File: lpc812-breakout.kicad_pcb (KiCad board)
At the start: 2 copper layers, 24 x 37.5 mm, 28 parts, among them J1 SWD, J2 Left, J3 Right, Q1 BC847BDW1, SW1 Reset, U1 LPC812M101JDH20, Y1 8MHz

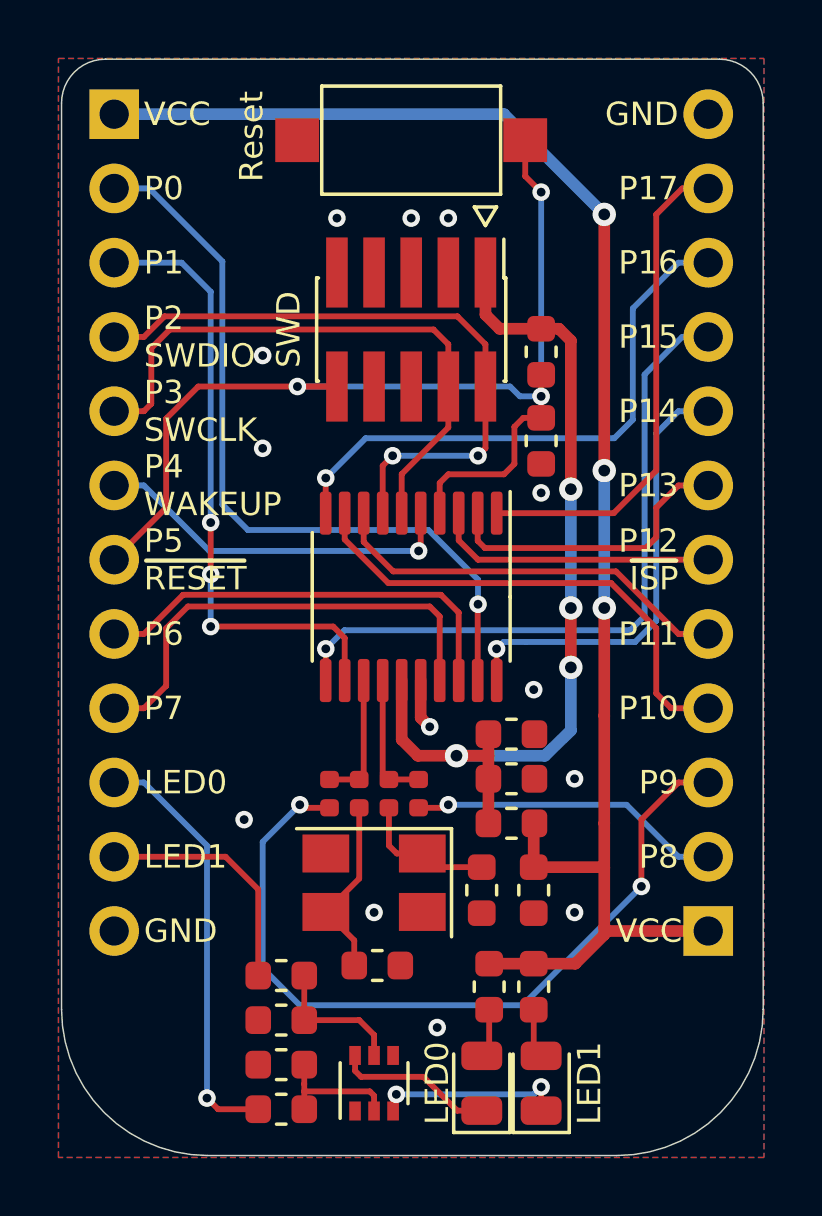
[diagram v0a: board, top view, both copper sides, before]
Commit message: PCB tweaks, updated documentation
- made the PCB a bit narrower: 24 mm -> 23 mm
- added/moved some of the GND vias
- updated docs and the BOM
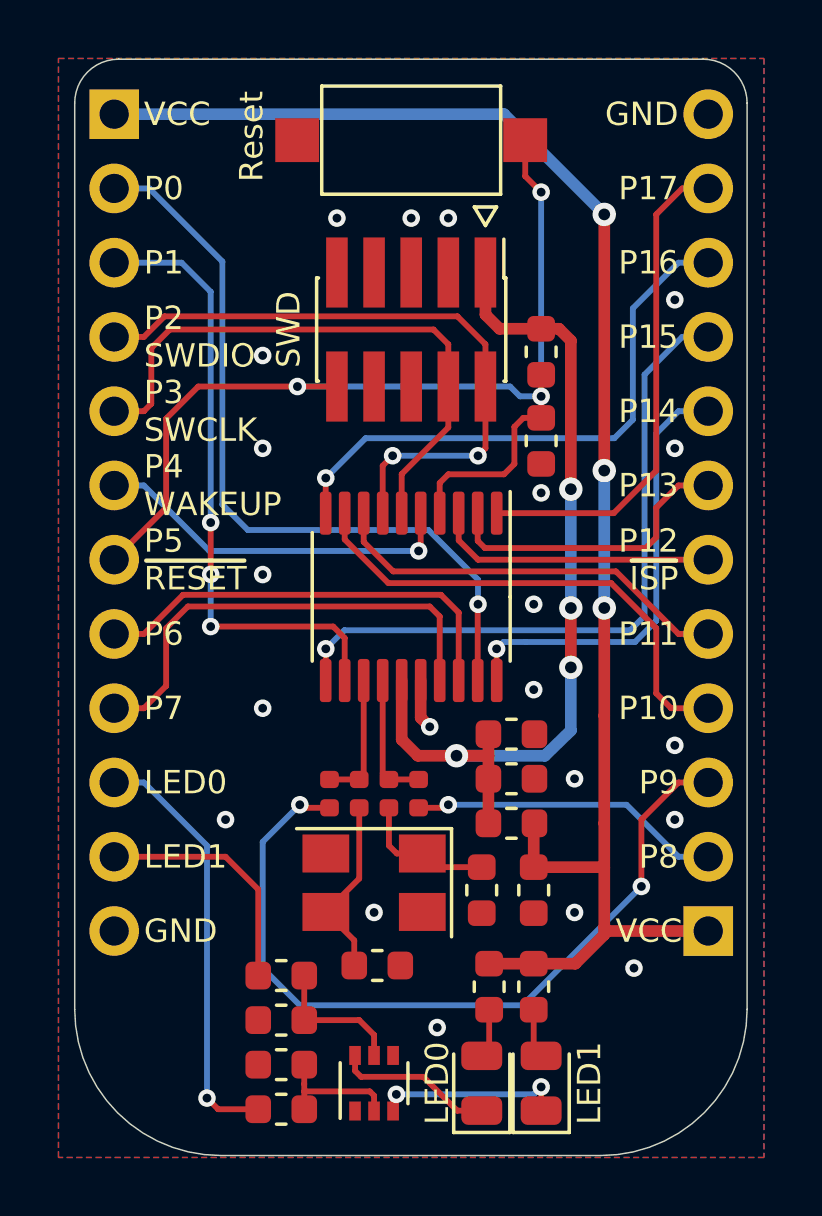
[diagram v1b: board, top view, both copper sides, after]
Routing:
- net GND: vias 13 -> 21
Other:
- board size 24 x 37.5 mm -> 23 x 37.5 mm

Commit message: More GND vias
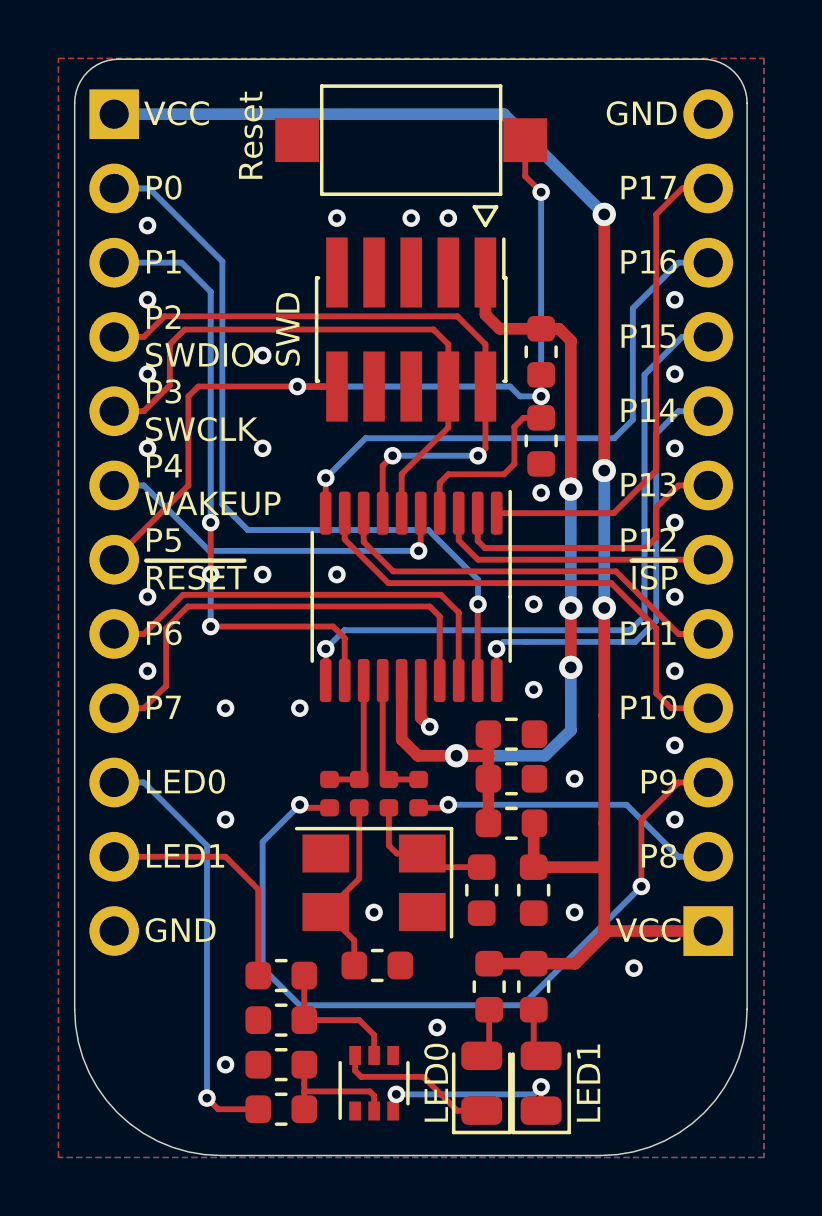
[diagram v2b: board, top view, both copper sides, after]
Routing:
- net GND: vias 21 -> 34
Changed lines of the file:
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@@
     (thickness 1.6)
     (drawings 40)
-    (tracks 273)
+    (tracks 286)
     (zones 0)
     (modules 28)
@@
   (via (at 146.177 92.71) (size 0.6) (drill 0.3) (layers F.Cu B.Cu) (net 1))
   (via (at 146.177 87.63) (size 0.6) (drill 0.3) (layers F.Cu B.Cu) (net 1))
-  (via (at 132.08 101.6) (size 0.6) (drill 0.3) (layers F.Cu B.Cu) (net 1))
+  (via (at 133.35 101.6) (size 0.6) (drill 0.3) (layers F.Cu B.Cu) (net 1))
   (via (at 132.08 97.028) (size 0.6) (drill 0.3) (layers F.Cu B.Cu) (net 1))
+  (via (at 134.62 97.028) (size 0.6) (drill 0.3) (layers F.Cu B.Cu) (net 1))
+  (via (at 130.81 101.6) (size 0.6) (drill 0.3) (layers F.Cu B.Cu) (net 1))
+  (via (at 128.143 97.79) (size 0.6) (drill 0.3) (layers F.Cu B.Cu) (net 1))
+  (via (at 128.143 100.33) (size 0.6) (drill 0.3) (layers F.Cu B.Cu) (net 1))
+  (via (at 128.143 92.71) (size 0.6) (drill 0.3) (layers F.Cu B.Cu) (net 1))
+  (via (at 128.143 87.63) (size 0.6) (drill 0.3) (layers F.Cu B.Cu) (net 1))
+  (via (at 128.143 85.09) (size 0.6) (drill 0.3) (layers F.Cu B.Cu) (net 1))
+  (via (at 146.177 97.79) (size 0.6) (drill 0.3) (layers F.Cu B.Cu) (net 1))
+  (via (at 146.177 100.33) (size 0.6) (drill 0.3) (layers F.Cu B.Cu) (net 1))
+  (via (at 146.177 95.25) (size 0.6) (drill 0.3) (layers F.Cu B.Cu) (net 1))
+  (via (at 146.177 90.17) (size 0.6) (drill 0.3) (layers F.Cu B.Cu) (net 1))
+  (via (at 128.143 90.17) (size 0.6) (drill 0.3) (layers F.Cu B.Cu) (net 1))
+  (via (at 130.81 113.792) (size 0.6) (drill 0.3) (layers F.Cu B.Cu) (net 1))
   (segment (start 136.398 105.006) (end 136.398 106.299) (width 0.2) (layer F.Cu) (net 2))
   (segment (start 136.668 106.569) (end 137.54 106.569) (width 0.2) (layer F.Cu) (net 2))
@@
   (segment (start 139.827 110.3375) (end 141.351 110.3375) (width 0.4) (layer F.Cu) (net 4))
   (segment (start 140.6905 93.2435) (end 140.335 93.599) (width 0.2) (layer F.Cu) (net 5))
-  (segment (start 128.778 94.742) (end 128.778 91.694) (width 0.2) (layer F.Cu) (net 5))
-  (segment (start 127 96.52) (end 128.778 94.742) (width 0.2) (layer F.Cu) (net 5))
-  (segment (start 129.876 90.596) (end 128.778 91.694) (width 0.2) (layer F.Cu) (net 5))
   (via (at 133.268 90.596) (size 0.6) (drill 0.3) (layers F.Cu B.Cu) (net 5))
-  (segment (start 133.268 90.596) (end 129.876 90.596) (width 0.2) (layer F.Cu) (net 5))
   (segment (start 134.62 90.596) (end 133.268 90.596) (width 0.2) (layer F.Cu) (net 5))
   (segment (start 140.6905 93.2435) (end 140.6905 91.9735) (width 0.2) (layer F.Cu) (net 5))
@@
   (segment (start 140.88 90.932) (end 140.544 90.596) (width 0.2) (layer B.Cu) (net 5))
   (segment (start 141.605 90.932) (end 140.88 90.932) (width 0.2) (layer B.Cu) (net 5))
+  (segment (start 129.54 90.932) (end 129.876 90.596) (width 0.2) (layer F.Cu) (net 5))
+  (segment (start 129.876 90.596) (end 133.268 90.596) (width 0.2) (layer F.Cu) (net 5))
+  (segment (start 129.54 93.98) (end 129.54 90.932) (width 0.2) (layer F.Cu) (net 5))
+  (segment (start 127 96.52) (end 129.54 93.98) (width 0.2) (layer F.Cu) (net 5))
   (segment (start 138.135 100.6525) (end 138.135 98.46004) (width 0.2) (layer F.Cu) (net 9))
   (segment (start 138.135 98.46004) (end 137.795 98.12004) (width 0.2) (layer F.Cu) (net 9))
@@
   (segment (start 138.43 91.996) (end 136.835 93.591) (width 0.2) (layer F.Cu) (net 12))
   (segment (start 138.43 90.596) (end 138.43 91.996) (width 0.2) (layer F.Cu) (net 12))
-  (segment (start 128.27 91.186) (end 128.016 91.44) (width 0.2) (layer F.Cu) (net 12))
-  (segment (start 128.27 89.281) (end 128.27 91.186) (width 0.2) (layer F.Cu) (net 12))
-  (segment (start 137.922 88.646) (end 128.905 88.646) (width 0.2) (layer F.Cu) (net 12))
+  (segment (start 128.905 90.551) (end 128.016 91.44) (width 0.2) (layer F.Cu) (net 12))
+  (segment (start 128.905 89.154) (end 128.905 90.551) (width 0.2) (layer F.Cu) (net 12))
   (segment (start 128.016 91.44) (end 127 91.44) (width 0.2) (layer F.Cu) (net 12))
-  (segment (start 128.905 88.646) (end 128.27 89.281) (width 0.2) (layer F.Cu) (net 12))
+  (segment (start 129.413 88.646) (end 128.905 89.154) (width 0.2) (layer F.Cu) (net 12))
+  (segment (start 137.922 88.646) (end 129.413 88.646) (width 0.2) (layer F.Cu) (net 12))
   (segment (start 138.43 89.154) (end 137.922 88.646) (width 0.2) (layer F.Cu) (net 12))
   (segment (start 138.43 90.596) (end 138.43 89.154) (width 0.2) (layer F.Cu) (net 12))
@@
   (segment (start 138.742001 88.196001) (end 139.7 89.154) (width 0.2) (layer F.Cu) (net 13))
   (segment (start 127 88.9) (end 128.016 88.9) (width 0.2) (layer F.Cu) (net 13))
-  (segment (start 129.306002 86.36) (end 130.302 87.355998) (width 0.2) (layer B.Cu) (net 14))
-  (segment (start 127 86.36) (end 129.306002 86.36) (width 0.2) (layer B.Cu) (net 14))
-  (via (at 130.302 95.25) (size 0.6) (drill 0.3) (layers F.Cu B.Cu) (net 14))
-  (segment (start 130.302 87.355998) (end 130.302 95.25) (width 0.2) (layer B.Cu) (net 14))
   (via (at 130.302 97.02003) (size 0.6) (drill 0.3) (layers F.Cu B.Cu) (net 14))
-  (segment (start 130.302 95.25) (end 130.302 97.02003) (width 0.2) (layer F.Cu) (net 14))
   (via (at 130.302 98.806) (size 0.6) (drill 0.3) (layers F.Cu B.Cu) (net 14))
   (segment (start 130.302 98.806) (end 130.302 97.02003) (width 0.2) (layer B.Cu) (net 14))
@@
   (segment (start 134.885 99.198) (end 134.885 100.6525) (width 0.2) (layer F.Cu) (net 14))
   (segment (start 134.493 98.806) (end 134.885 99.198) (width 0.2) (layer F.Cu) (net 14))
-  (segment (start 130.70201 86.319929) (end 128.202081 83.82) (width 0.2) (layer B.Cu) (net 15))
-  (segment (start 130.70201 94.63401) (end 130.70201 86.319929) (width 0.2) (layer B.Cu) (net 15))
-  (segment (start 137.749665 95.504) (end 131.572 95.504) (width 0.2) (layer B.Cu) (net 15))
-  (segment (start 128.202081 83.82) (end 127 83.82) (width 0.2) (layer B.Cu) (net 15))
-  (segment (start 131.572 95.504) (end 130.70201 94.63401) (width 0.2) (layer B.Cu) (net 15))
+  (via (at 130.302 95.25) (size 0.6) (drill 0.3) (layers F.Cu B.Cu) (net 14))
+  (segment (start 130.302 87.355998) (end 130.302 95.25) (width 0.2) (layer B.Cu) (net 14))
+  (segment (start 130.302 95.25) (end 130.302 97.02003) (width 0.2) (layer F.Cu) (net 14))
+  (segment (start 129.306002 86.36) (end 130.302 87.355998) (width 0.2) (layer B.Cu) (net 14))
+  (segment (start 127 86.36) (end 129.306002 86.36) (width 0.2) (layer B.Cu) (net 14))
   (via (at 139.446 98.044) (size 0.6) (drill 0.3) (layers F.Cu B.Cu) (net 15))
   (segment (start 139.435 98.055) (end 139.446 98.044) (width 0.2) (layer F.Cu) (net 15))
   (segment (start 139.435 100.6525) (end 139.435 98.055) (width 0.2) (layer F.Cu) (net 15))
+  (segment (start 139.446 98.044) (end 139.446 97.200335) (width 0.2) (layer B.Cu) (net 15))
   (segment (start 139.446 97.200335) (end 137.749665 95.504) (width 0.2) (layer B.Cu) (net 15))
-  (segment (start 139.446 98.044) (end 139.446 97.200335) (width 0.2) (layer B.Cu) (net 15))
+  (segment (start 130.70201 94.63401) (end 130.70201 86.319929) (width 0.2) (layer B.Cu) (net 15))
+  (segment (start 137.749665 95.504) (end 131.572 95.504) (width 0.2) (layer B.Cu) (net 15))
+  (segment (start 131.572 95.504) (end 130.70201 94.63401) (width 0.2) (layer B.Cu) (net 15))
+  (segment (start 130.70201 86.319929) (end 128.202081 83.82) (width 0.2) (layer B.Cu) (net 15))
+  (segment (start 128.202081 83.82) (end 127 83.82) (width 0.2) (layer B.Cu) (net 15))
   (segment (start 140.085 94.9275) (end 144.0865 94.9275) (width 0.2) (layer F.Cu) (net 16))
   (segment (start 144.0865 94.9275) (end 145.542 93.472) (width 0.2) (layer F.Cu) (net 16))

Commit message: Project upgrade to KiCad 6
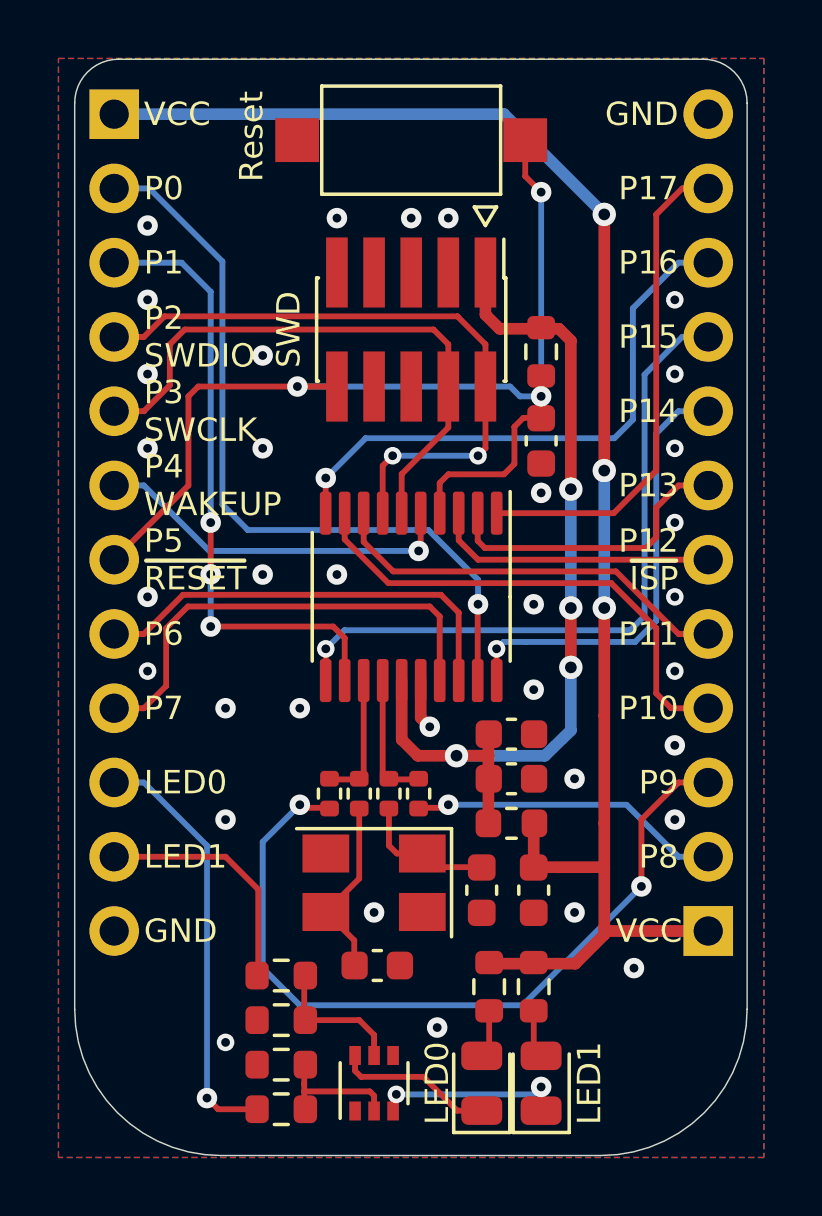
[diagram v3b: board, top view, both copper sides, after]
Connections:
- net /~RESET renamed /~{RESET}
- J1 pad 6: Net-(J1-Pad6) -> unconnected-(J1-Pad6)
- J1 pad 7: Net-(J1-Pad7) -> unconnected-(J1-Pad7)
- J1 pad 8: Net-(J1-Pad8) -> unconnected-(J1-Pad8)
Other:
- net class Default removed
- net class Ground removed
- net class Power removed
- board text added: "P12 ~{ISP}"
- board text added: "P5 ~{RESET}"
- board text removed: "P12 ~ISP"
- board text removed: "P5 ~RESET"
